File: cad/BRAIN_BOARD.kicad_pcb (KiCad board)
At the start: 4 copper layers, 99.5 x 92.2 mm, 128 parts, among them J1 VH, J10 PH-3, J11 640454-4, J2 USB4105-GF-A (USB-C), J3 ZH-3, J4 MTA-5, J5 TC2030-NL, J6 MTA-8, J7 ZH-3, J8 1040310811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

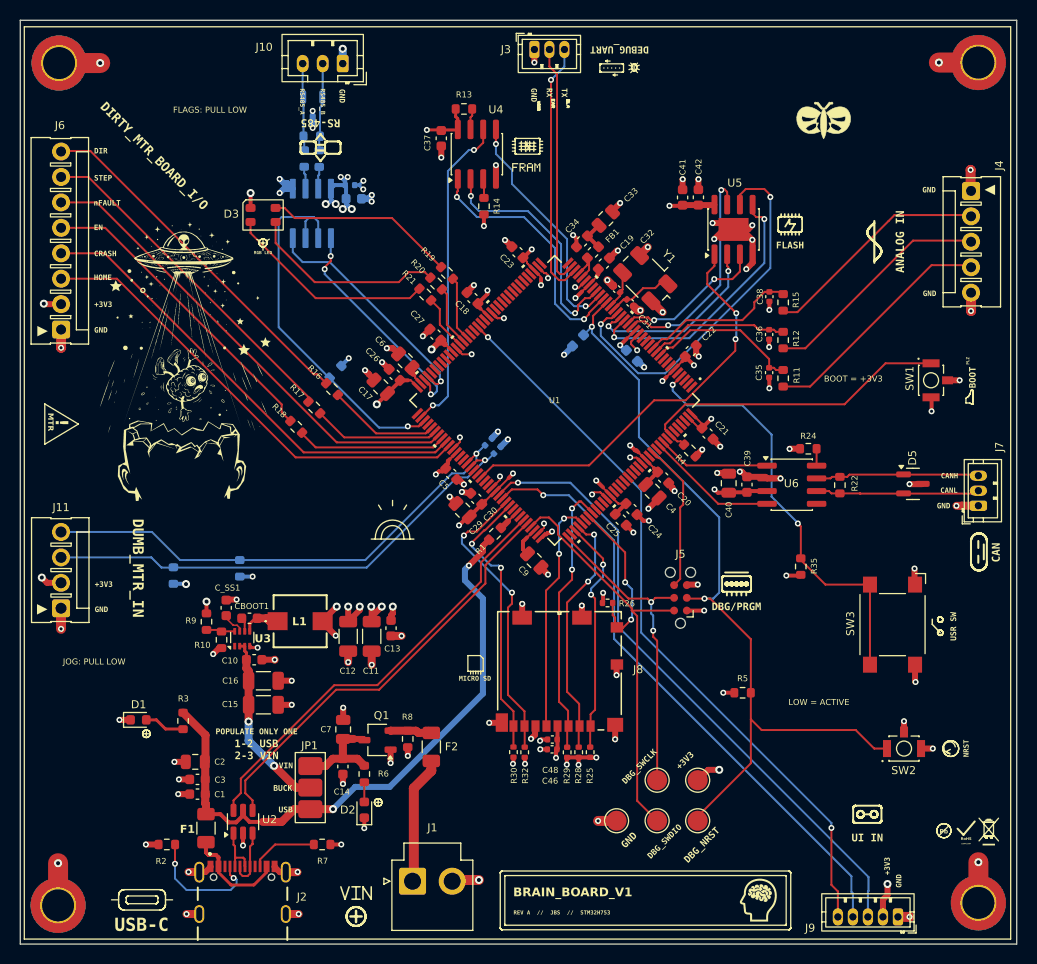
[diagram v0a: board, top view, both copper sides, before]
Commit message: removed EH connectors
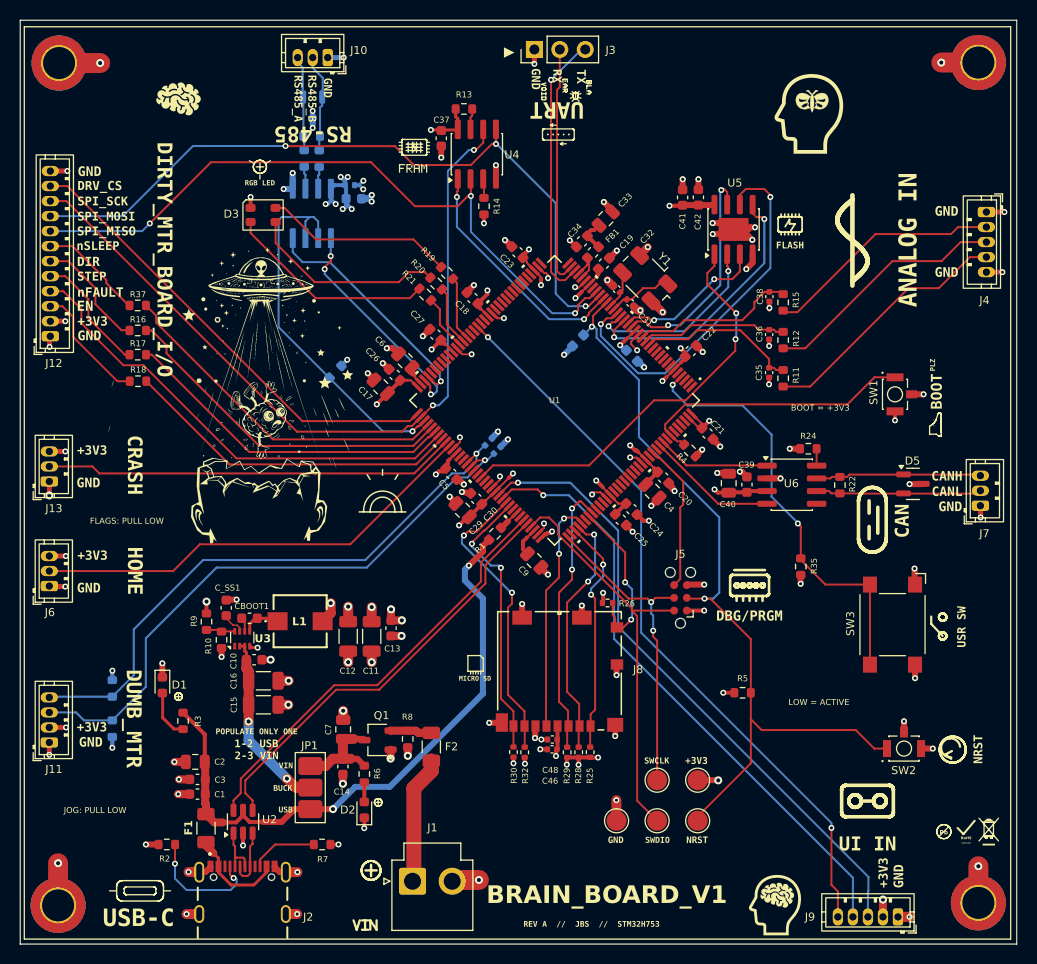
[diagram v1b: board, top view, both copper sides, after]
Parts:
- added J12: JST_EH-14, JST_ZH:JST_ZH_B12B-ZR_1x12_P1.50mm_Vertical, F.Cu at (17.0, 135.3)
- added J13: CRASH, JST_ZH:JST_ZH_B3B-ZR_1x03_P1.50mm_Vertical, F.Cu at (16.9, 149.8)
- added R37: 100, RESISTOR:R_0603, F.Cu at (25.7, 132.2)
- J10: footprint JST_PH:JST_PH_B3B-PH-K_1x03_P2.00mm_Vertical -> JST_ZH:JST_ZH_B3B-ZR_1x03_P1.50mm_Vertical
- J11: value 640454-4 -> MTA-4; footprint MTA:MTA-4 -> JST_ZH:JST_ZH_B4B-ZR_1x04_P1.50mm_Vertical
- J3: footprint JST_ZH:JST_ZH_B3B-ZR_1x03_P1.50mm_Vertical -> PIN_HEADER:PinHeader_1x03_P2.54mm_Vertical
- J4: footprint MTA:MTA-5 -> JST_ZH:JST_ZH_B5B-ZR_1x05_P1.50mm_Vertical
- J6: value MTA-8 -> HOME; footprint MTA:MTA-8 -> JST_ZH:JST_ZH_B3B-ZR_1x03_P1.50mm_Vertical
- moved J6 34.5 mm to (16.9, 160.3), turned to 90 degrees
- moved J11 23.6 mm to (16.9, 175.9), turned to 90 degrees
- moved R16 20.3 mm to (25.7, 134.7), turned to 180 degrees
- moved R17 18.4 mm to (25.7, 137.1), turned to 180 degrees
- moved R31 17.5 mm to (23.2, 170.5), turned to -90 degrees
- moved R33 16.5 mm to (23.2, 174.5)
- moved R18 16.4 mm to (25.8, 139.8), turned to 180 degrees
- moved J4 8.19 mm to (110.5, 122.9), turned to -90 degrees
- moved D1 4.22 mm to (28.2, 170.1), turned to -90 degrees
- moved SW1 3.86 mm to (101.3, 141.1)
- moved J10 1.62 mm to (44.7, 107.5)
- moved J7 0.20 mm to (109.9, 152.2)
- turned J3 to 90 degrees
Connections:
- net /BRAIN_BOARD/FRAM_MISO renamed /BRAIN_BOARD/SPI_MISO
- net /BRAIN_BOARD/FRAM_MOSI renamed /BRAIN_BOARD/SPI_MOSI
- net /BRAIN_BOARD/FRAM_SCK renamed /BRAIN_BOARD/SPI_SCK
- J6 pad 2: +3.3V -> /BRAIN_BOARD/HOME_FLAG
- J6 pad 3: /BRAIN_BOARD/HOME_FLAG -> +3.3V
- R16 pad 2: Net-(J6-Pin_8) -> /BRAIN_BOARD/DIR_MTR
- R17 pad 2: Net-(J6-Pin_7) -> /BRAIN_BOARD/STEP_MTR
- R18 pad 2: Net-(J6-Pin_5) -> /BRAIN_BOARD/ENABLE_MTR
- U1 pad 10: /BRAIN_BOARD/ADC_CURRENT_SENSE -> unconnected-(U1B-PF0-Pad10)
- U1 pad 11: /BRAIN_BOARD/ADC_24V_SENSE -> unconnected-(U1B-PF1-Pad11)
- U1 pad 12: /BRAIN_BOARD/ADC_5V_SENSE -> unconnected-(U1B-PF2-Pad12)
- U1 pad 13: unconnected-(U1B-PF3-Pad13) -> /BRAIN_BOARD/ADC_CURRENT_SENSE
- U1 pad 14: unconnected-(U1B-PF4-Pad14) -> /BRAIN_BOARD/ADC_24V_SENSE
- U1 pad 15: unconnected-(U1B-PF5-Pad15) -> /BRAIN_BOARD/ADC_5V_SENSE
- U1 pad 73: unconnected-(U1A-PB12-Pad73) -> /BRAIN_BOARD/DRV_CS
- U1 pad 76: unconnected-(U1A-PB15-Pad76) -> Net-(U1A-PB15)
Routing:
- net /BRAIN_BOARD/SPI_MOSI: track 23.9 -> 73.3 mm, vias 2 -> 3
- net /BRAIN_BOARD/SPI_SCK: track 32.5 -> 79.2 mm
- net /BRAIN_BOARD/DRV_CS: track 0.00 -> 46.7 mm
- net /BRAIN_BOARD/SPI_MISO: track 24.1 -> 69.5 mm, vias 2 -> 3
- net Net-(J6-Pin_8): track 36.1 -> 0.00 mm
- net Net-(U1A-PB15): track 0.00 -> 34.7 mm
- net Net-(J6-Pin_7): track 34.3 -> 0.00 mm
- net Net-(J6-Pin_5): track 31.4 -> 0.00 mm
- net /BRAIN_BOARD/DIR: track 11.2 -> 34.5 mm
- net /BRAIN_BOARD/STEP: track 12.7 -> 33.8 mm
- net /BRAIN_BOARD/ENABLE: track 15.1 -> 34.1 mm
- net /BRAIN_BOARD/STEP_MTR: track 0.00 -> 12.3 mm
- net /BRAIN_BOARD/ENABLE_MTR: track 0.00 -> 12.2 mm
- net /BRAIN_BOARD/DIR_MTR: track 0.00 -> 11.7 mm
- net /BRAIN_BOARD/MTR_nSLEEP: track 0.00 -> 10.5 mm
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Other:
- board text added: "▼"
